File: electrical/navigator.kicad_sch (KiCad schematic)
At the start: 5 parts

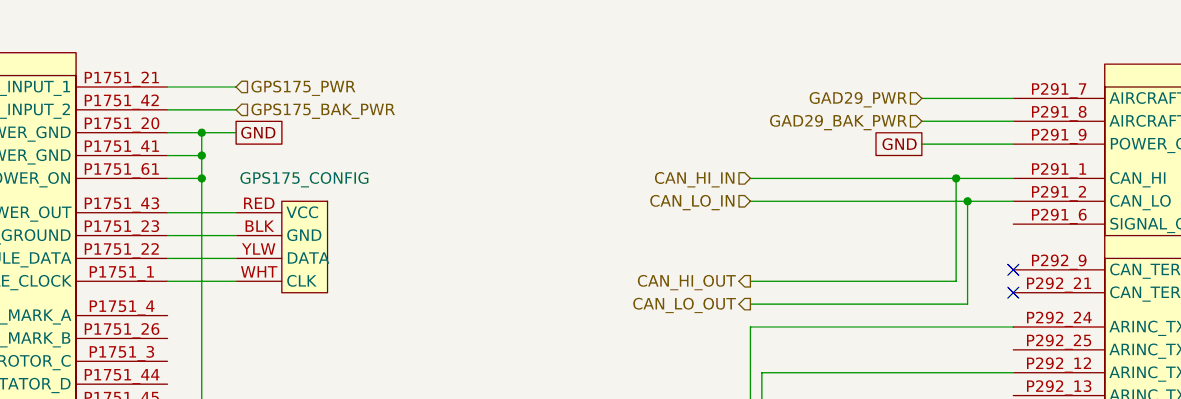
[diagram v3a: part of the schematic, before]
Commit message: Updated electrical to not use IBBS. Also, added BT adapter and 3P3T switch.
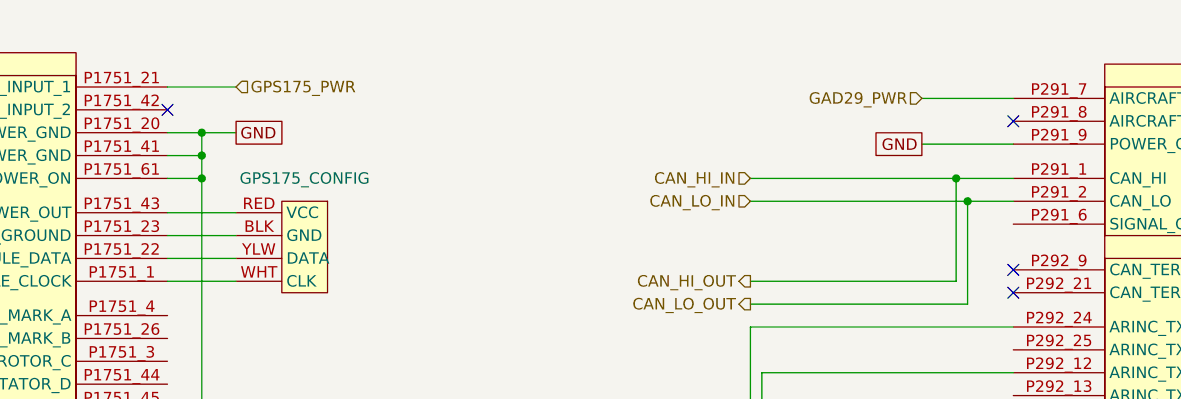
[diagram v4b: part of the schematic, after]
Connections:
- net GAD29_BAK_PWR: no longer names the net of GAD29.P291_8 (AIRCRAFT_POWER_2)
- net GPS175_BAK_PWR: no longer names the net of GPS175.P1751_42 (POWER_INPUT_2)
- no-connect marks 2 -> 4
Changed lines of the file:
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@@
   (junction (at 68.58 29.21) (diameter 0) (color 0 0 0 0)
   )
+  (no_connect (at 158.75 25.4))
+  (no_connect (at 64.77 24.13))
   (no_connect (at 158.75 44.45))
   (no_connect (at 158.75 41.91))
@@
     (stroke (width 0) (type default))
   )
-  (wire (pts (xy 148.59 25.4) (xy 158.75 25.4))
-    (stroke (width 0) (type default))
-  )
   (wire (pts (xy 64.77 86.36) (xy 73.66 86.36))
     (stroke (width 0) (type default))
@@
   )
   (wire (pts (xy 73.66 175.26) (xy 73.66 172.72))
-    (stroke (width 0) (type default))
-  )
-  (wire (pts (xy 64.77 24.13) (xy 72.39 24.13))
     (stroke (width 0) (type default))
   )
@@
     (effects (font (size 1.27 1.27)) (justify left))
   )
-  (hierarchical_label "GPS175_BAK_PWR" (shape input) (at 72.39 24.13 0) (fields_autoplaced)
-    (effects (font (size 1.27 1.27)) (justify left))
-  )
   (hierarchical_label "CAN_LO_IN" (shape input) (at 129.54 34.29 180) (fields_autoplaced)
     (effects (font (size 1.27 1.27)) (justify right))
@@
     (effects (font (size 1.27 1.27)) (justify left))
   )
-  (hierarchical_label "GAD29_BAK_PWR" (shape input) (at 148.59 25.4 180) (fields_autoplaced)
-    (effects (font (size 1.27 1.27)) (justify right))
-  )
   (hierarchical_label "TOGA_OUT" (shape output) (at 76.2 175.26 0) (fields_autoplaced)

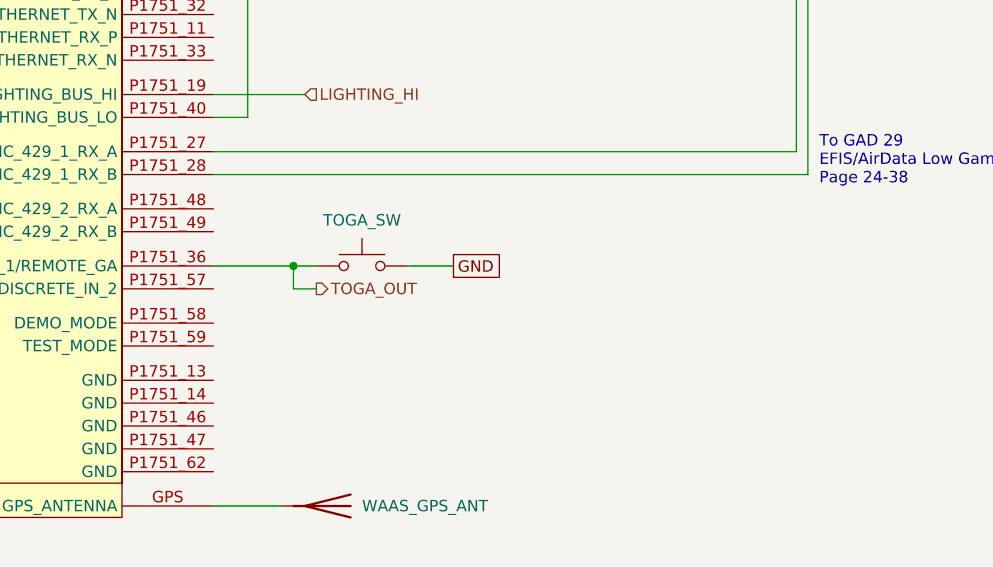
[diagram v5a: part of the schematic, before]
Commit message: Added AV breaker. Added diodes to TOGA. Moved smoke to use roll trim. Changec cabin & panel to use a single fuse.
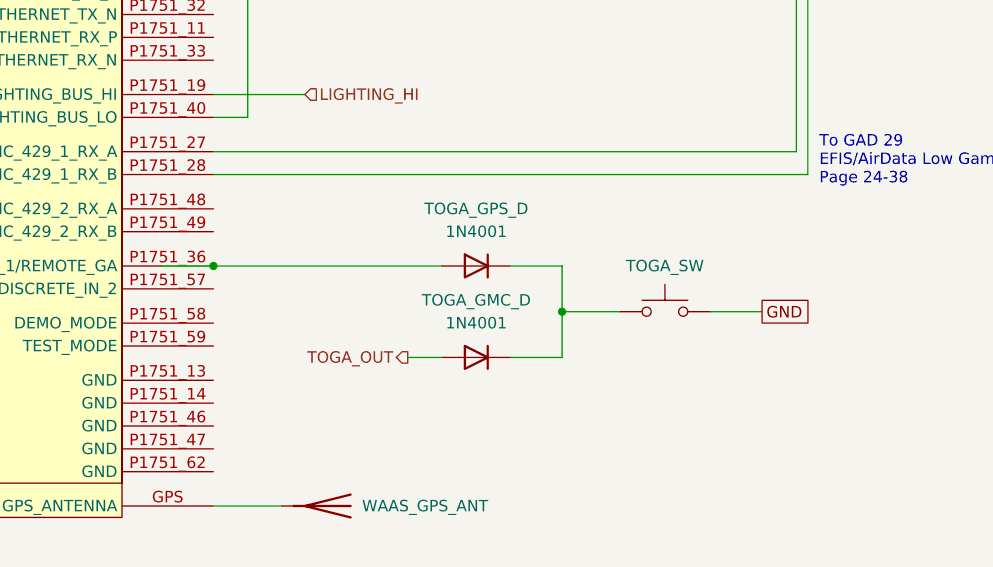
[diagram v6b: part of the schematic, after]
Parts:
- added TOGA_GMC_D, TOGA_GPS_D: 1N4001, Diode_THT:D_DO-41_SOD81_P10.16mm_Horizontal, symbol Diode:1N4001
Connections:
- net TOGA_OUT: now also TOGA_GMC_D.2 (A); no longer GPS175.P1751_36 (DISCRETE_IN_1/REMOTE_GA), TOGA_SW.1
- new net: TOGA_GMC_D.1 (K), TOGA_GPS_D.1 (K), TOGA_SW.1
- new net: GPS175.P1751_36 (DISCRETE_IN_1/REMOTE_GA), TOGA_GPS_D.2 (A)
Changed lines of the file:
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@@
   (paper "A" portrait)
   (title_block
-    (date "2024-05-07")
-    (rev "1.0")
+    (date "2024-05-21")
+    (rev "1.0.3")
     (company "N877RV")
   )
+  (junction (at 103.505 177.8) (diameter 0) (color 0 0 0 0)
+  )
   (junction (at 68.58 31.75) (diameter 0) (color 0 0 0 0)
   )
   (junction (at 152.4 31.75) (diameter 0) (color 0 0 0 0)
   )
+  (junction (at 64.77 172.72) (diameter 0) (color 0 0 0 0)
+  )
   (junction (at 153.67 34.29) (diameter 0) (color 0 0 0 0)
-  )
-  (junction (at 73.66 172.72) (diameter 0) (color 0 0 0 0)
   )
   (junction (at 68.58 26.67) (diameter 0) (color 0 0 0 0)
@@
     (stroke (width 0) (type default))
   )
-  (wire (pts (xy 64.77 172.72) (xy 73.66 172.72))
+  (wire (pts (xy 59.055 172.72) (xy 64.77 172.72))
     (stroke (width 0) (type default))
   )
@@
     (stroke (width 0) (type default))
   )
+  (wire (pts (xy 120.015 177.8) (xy 125.73 177.8))
+    (stroke (width 0) (type default))
+  )
   (wire (pts (xy 130.81 53.34) (xy 158.75 53.34))
     (stroke (width 0) (type default))
   )
-  (wire (pts (xy 73.66 172.72) (xy 76.2 172.72))
-    (stroke (width 0) (type default))
-  )
   (wire (pts (xy 130.81 162.56) (xy 130.81 53.34))
     (stroke (width 0) (type default))
   )
+  (wire (pts (xy 103.505 182.88) (xy 103.505 177.8))
+    (stroke (width 0) (type default))
+  )
   (wire (pts (xy 129.54 43.18) (xy 152.4 43.18))
     (stroke (width 0) (type default))
@@
     (stroke (width 0) (type default))
   )
+  (wire (pts (xy 64.77 172.72) (xy 90.17 172.72))
+    (stroke (width 0) (type default))
+  )
   (wire (pts (xy 68.58 156.21) (xy 68.58 31.75))
     (stroke (width 0) (type default))
@@
     (stroke (width 0) (type default))
   )
+  (wire (pts (xy 103.505 172.72) (xy 103.505 177.8))
+    (stroke (width 0) (type default))
+  )
   (wire (pts (xy 129.54 45.72) (xy 153.67 45.72))
     (stroke (width 0) (type default))
@@
     (stroke (width 0) (type default))
   )
+  (wire (pts (xy 97.79 172.72) (xy 103.505 172.72))
+    (stroke (width 0) (type default))
+  )
   (wire (pts (xy 152.4 43.18) (xy 152.4 31.75))
     (stroke (width 0) (type default))
   )
-  (wire (pts (xy 73.66 175.26) (xy 73.66 172.72))
+  (wire (pts (xy 86.36 182.88) (xy 90.17 182.88))
     (stroke (width 0) (type default))
   )
@@
     (stroke (width 0) (type default))
   )
-  (wire (pts (xy 86.36 172.72) (xy 91.44 172.72))
-    (stroke (width 0) (type default))
-  )
   (wire (pts (xy 140.97 68.58) (xy 140.97 71.12))
     (stroke (width 0) (type default))
@@
     (stroke (width 0) (type default))
   )
+  (wire (pts (xy 103.505 177.8) (xy 109.855 177.8))
+    (stroke (width 0) (type default))
+  )
   (wire (pts (xy 64.77 31.75) (xy 68.58 31.75))
     (stroke (width 0) (type default))
@@
     (stroke (width 0) (type default))
   )
-  (wire (pts (xy 76.2 175.26) (xy 73.66 175.26))
-    (stroke (width 0) (type default))
-  )
   (wire (pts (xy 64.77 29.21) (xy 68.58 29.21))
     (stroke (width 0) (type default))
   )
   (wire (pts (xy 148.59 27.94) (xy 158.75 27.94))
+    (stroke (width 0) (type default))
+  )
+  (wire (pts (xy 97.79 182.88) (xy 103.505 182.88))
     (stroke (width 0) (type default))
   )
@@
     )
   )
-  (global_label "GND" (shape passive) (at 91.44 172.72 0) (fields_autoplaced)
-    (effects (font (size 1.27 1.27)) (justify left))
-    (property "Intersheetrefs" "${INTERSHEET_REFS}" (at 97.1844 172.72 0)
+  (global_label "GND" (shape passive) (at 125.73 177.8 0) (fields_autoplaced)
+    (effects (font (size 1.27 1.27)) (justify left))
+    (property "Intersheetrefs" "${INTERSHEET_REFS}" (at 131.4744 177.8 0)
       (effects (font (size 1.27 1.27)) (justify left) hide)
     )
@@
     (effects (font (size 1.27 1.27)) (justify left))
   )
-  (hierarchical_label "TOGA_OUT" (shape output) (at 76.2 175.26 0) (fields_autoplaced)
-    (effects (font (size 1.27 1.27)) (justify left))
+  (hierarchical_label "TOGA_OUT" (shape output) (at 86.36 182.88 180) (fields_autoplaced)
+    (effects (font (size 1.27 1.27)) (justify right))
   )
   (symbol (lib_id "flyerx:Garmin_Config") (at 82.55 34.29 0) (mirror y) (unit 1)
@@
         (path "/e8ec215a-dbe2-4eba-a577-e50a0a128049/a7d1a714-f940-4397-adef-d76b5058aa57"
           (reference "GPS175_CONFIG") (unit 1)
+        )
+      )
+    )
+  )
+  (symbol (lib_id "Diode:1N4001") (at 93.98 182.88 0) (mirror y) (unit 1)
+    (in_bom yes) (on_board yes) (dnp no)
+    (property "Reference" "TOGA_GMC_D" (at 93.98 176.53 0)
+      (effects (font (size 1.27 1.27)))
+    )
+    (property "Value" "1N4001" (at 93.98 179.07 0)
+      (effects (font (size 1.27 1.27)))
+    )
+    (property "Footprint" "Diode_THT:D_DO-41_SOD81_P10.16mm_Horizontal" (at 93.98 182.88 0)
+      (effects (font (size 1.27 1.27)) hide)
+    )
+    (property "Datasheet" "http://www.vishay.com/docs/88503/1n4001.pdf" (at 93.98 182.88 0)
+      (effects (font (size 1.27 1.27)) hide)
+    )
+    (property "Sim.Device" "D" (at 93.98 182.88 0)
+      (effects (font (size 1.27 1.27)) hide)
+    )
+    (property "Sim.Pins" "1=K 2=A" (at 93.98 182.88 0)
+      (effects (font (size 1.27 1.27)) hide)
+    )
+    (pin "2")
+    (pin "1")
+    (instances
+      (project "electrical"
+        (path "/e8ec215a-dbe2-4eba-a577-e50a0a128049/a7d1a714-f940-4397-adef-d76b5058aa57"
+          (reference "TOGA_GMC_D") (unit 1)
+        )
+      )
+    )
+  )
+  (symbol (lib_id "Switch:SW_Push") (at 114.935 177.8 0) (unit 1)
+    (in_bom yes) (on_board yes) (dnp no)
+    (property "Reference" "TOGA_SW" (at 114.935 172.72 0)
+      (effects (font (size 1.27 1.27)))
+    )
+    (property "Value" "SW_Push" (at 114.935 172.72 0)
+      (effects (font (size 1.27 1.27)) hide)
+    )
+    (property "Footprint" "" (at 114.935 172.72 0)
+      (effects (font (size 1.27 1.27)) hide)
+    )
+    (property "Datasheet" "~" (at 114.935 172.72 0)
+      (effects (font (size 1.27 1.27)) hide)
+    )
+    (pin "1")
+    (pin "2")
+    (instances
+      (project "electrical"
+        (path "/e8ec215a-dbe2-4eba-a577-e50a0a128049/a7d1a714-f940-4397-adef-d76b5058aa57"
+          (reference "TOGA_SW") (unit 1)
         )
       )
@@
     )
   )
-  (symbol (lib_id "Switch:SW_Push") (at 81.28 172.72 0) (unit 1)
+  (symbol (lib_id "Diode:1N4001") (at 93.98 172.72 0) (mirror y) (unit 1)
     (in_bom yes) (on_board yes) (dnp no)
-    (property "Reference" "TOGA_SW" (at 81.28 167.64 0)
-      (effects (font (size 1.27 1.27)))
-    )
-    (property "Value" "SW_Push" (at 81.28 167.64 0)
-      (effects (font (size 1.27 1.27)) hide)
-    )
-    (property "Footprint" "" (at 81.28 167.64 0)
-      (effects (font (size 1.27 1.27)) hide)
-    )
-    (property "Datasheet" "~" (at 81.28 167.64 0)
-      (effects (font (size 1.27 1.27)) hide)
-    )
+    (property "Reference" "TOGA_GPS_D" (at 93.98 166.37 0)
+      (effects (font (size 1.27 1.27)))
+    )
+    (property "Value" "1N4001" (at 93.98 168.91 0)
+      (effects (font (size 1.27 1.27)))
+    )
+    (property "Footprint" "Diode_THT:D_DO-41_SOD81_P10.16mm_Horizontal" (at 93.98 172.72 0)
+      (effects (font (size 1.27 1.27)) hide)
+    )
+    (property "Datasheet" "http://www.vishay.com/docs/88503/1n4001.pdf" (at 93.98 172.72 0)
+      (effects (font (size 1.27 1.27)) hide)
+    )
+    (property "Sim.Device" "D" (at 93.98 172.72 0)
+      (effects (font (size 1.27 1.27)) hide)
+    )
+    (property "Sim.Pins" "1=K 2=A" (at 93.98 172.72 0)
+      (effects (font (size 1.27 1.27)) hide)
+    )
+    (pin "2")
     (pin "1")
-    (pin "2")
-    (instances
-      (project "electrical"
-        (path "/e8ec215a-dbe2-4eba-a577-e50a0a128049/a7d1a714-f940-4397-adef-d76b5058aa57"
-          (reference "TOGA_SW") (unit 1)
-        )
-      )
+    (instances
+      (project "electrical"
+        (path "/e8ec215a-dbe2-4eba-a577-e50a0a128049/a7d1a714-f940-4397-adef-d76b5058aa57"
+          (reference "TOGA_GPS_D") (unit 1)
+        )
+      )
